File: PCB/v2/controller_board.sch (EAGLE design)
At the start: 30 parts, among them M1 B4B-PH-K-S(LF)(SN), M2 B4B-PH-K-S(LF)(SN), M3 B4B-PH-K-S(LF)(SN), M4 B4B-PH-K-S(LF)(SN)

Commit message: chore(pcb): improve schematics
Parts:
- added R8: 10kR, rcl:R-EU_R0805
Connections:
- net A3 renamed N$24
- removed net N$24 (its old number): D2.A, POWER_CONNECTOR.1
- removed net N$26: D1.A, POWER_CONNECTOR.4
- new net N$22: CONTROLLER.5, R1.2, R8.1, UART_1.2
- net GND: now also D1.A, D2.A, POWER_CONNECTOR.1, POWER_CONNECTOR.4; no longer MC4.!EN
- net UART: now also R8.2; no longer CONTROLLER.5, R1.2, UART_1.2
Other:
- moved on the sheet: 24V_FUSE, 5V_FUSE, CONTROLLER, D1, D2, DEBUG, I2C_1, LED, M1, M2, M3, M4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

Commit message: feat(pcb): add ESD protection
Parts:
- removed DEBUG: B2B-PH-K-S(LF)(SN), B2B-PH-K-S_LF__SN_:B2B-PH-K-S(LF)(SN)
- removed MC1, MC2, MC3, MC4: TMC2209_SILENTSTEPSTICK, TMC2209_SILENTSTEPSTICK:TMC2209_SILENTSTEPSTICK
- added C_M1_A1, C_M1_A2, C_M1_B1, C_M1_B2, C_M2_A1, C_M2_A2, C_M2_A3, C_M2_A4, C_M2_B1, C_M2_B2, C_M2_B3, C_M2_B4, C_M3_A1, C_M3_A2, C_M3_B1, C_M3_B2: 470pF 100V, rcl:C-EUC0402
- added L_M1_A1, L_M1_A2, L_M1_B1, L_M1_B2, L_M2_A1, L_M2_A2, L_M2_A3, L_M2_A4, L_M2_B1, L_M2_B2, L_M2_B3, L_M2_B4, L_M3_A1, L_M3_A2, L_M3_B1, L_M3_B2: 50Ohm@100MHz, ngspice-simulation:L
- added M1_TMC, M2_TMC, M3_TMC, M4_TMC: TMC2209_SILENTSTEPSTICK, TMC2209_SILENTSTEPSTICK:TMC2209_SILENTSTEPSTICK
- added R_M1_A, R_M1_B, R_M2_A, R_M2_A1, R_M2_B, R_M2_B1, R_M3_A, R_M3_B: S1210, varistor:S1210
- CONTROLLER: value TINY2040 -> TINY2040_HEADER; device pimoroni-boards:TINY2040 -> tiny2040_headerd:TINY2040_HEADER
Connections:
- removed net N$18 (its old number): CONTROLLER.SWCLK, DEBUG.2
- new net N$19: L_M1_A2.1, M1_TMC.M2A
- new net N$26: L_M1_A1.1, M1_TMC.M1A
- new net N$27: L_M1_B2.1, M1_TMC.M2B
- new net N$28: L_M2_A1.1, M2_TMC.M1A
- new net N$29: L_M2_A2.1, M2_TMC.M2A
- new net N$30: L_M2_B2.1, M2_TMC.M2B
- new net N$31: L_M2_B1.1, M2_TMC.M1B
- new net N$32: C_M2_A3.2, L_M2_A3.2, M4.1, R_M2_A1.1
- new net N$33: C_M2_A4.2, L_M2_A4.2, M4.2, R_M2_A1.2
- new net N$34: C_M2_B3.2, L_M2_B3.2, M4.3, R_M2_B1.1
- new net N$35: C_M2_B4.2, L_M2_B4.2, M4.4, R_M2_B1.2
- new net N$36: L_M2_A3.1, M4_TMC.M1A
- new net N$37: L_M2_A4.1, M4_TMC.M2A
- new net N$38: L_M2_B4.1, M4_TMC.M2B
- new net N$39: L_M2_B3.1, M4_TMC.M1B
- net 24V: now also M1_TMC.VM, M2_TMC.VM, M3_TMC.VM, M4_TMC.VM; no longer MC1.VM, MC2.VM, MC3.VM, MC4.VM
- net 5V: now also M1_TMC.VIO, M2_TMC.MS1, M2_TMC.VIO, M3_TMC.MS2, M3_TMC.VIO, M4_TMC.MS1, M4_TMC.MS2, M4_TMC.VIO; no longer MC1.VIO, MC2.MS1, MC2.VIO, MC3.MS2, MC3.VIO, MC4.MS1, MC4.MS2, MC4.VIO
- net GND: now also CONTROLLER.GND2, CONTROLLER.GND3, C_M1_A1.1, C_M1_A2.1, C_M1_B1.1, C_M1_B2.1, C_M2_A1.1, C_M2_A2.1, C_M2_A3.1, C_M2_A4.1, C_M2_B1.1, C_M2_B2.1, C_M2_B3.1, C_M2_B4.1, C_M3_A1.1, C_M3_A2.1, C_M3_B1.1, C_M3_B2.1, M1_TMC.!EN, M1_TMC.GND, M1_TMC.MS1, M1_TMC.MS2, M2_TMC.!EN, M2_TMC.GND, M2_TMC.MS2, M3_TMC.!EN, M3_TMC.GND, M3_TMC.MS1, M4_TMC.GND; no longer MC1.!EN, MC1.GND, MC1.MS1, MC1.MS2, MC2.!EN, MC2.GND, MC2.MS2, MC3.!EN, MC3.GND, MC3.MS1, MC4.GND
- net N$1: now also C_M1_A1.2, L_M1_A1.2, R_M1_A.1; no longer MC1.M2A
- net N$10: now also C_M3_A2.2, L_M3_A2.2, M3.2, R_M3_A.2; no longer M3.4, MC3.M1A
- net N$11: now also C_M3_B1.2, L_M3_B1.2, M3.3, R_M3_B.1; no longer M3.2, MC3.M2B
- net N$12: now also C_M3_B2.2, L_M3_B2.2, M3.4, R_M3_B.2; no longer M3.3, MC3.M1B
- net N$13: now also L_M3_A1.1, M3_TMC.M1A; no longer M4.1, MC4.M2A
- net N$14: now also L_M3_A2.1, M3_TMC.M2A; no longer M4.4, MC4.M1A
- net N$15: now also L_M3_B2.1, M3_TMC.M2B; no longer M4.2, MC4.M2B
- net N$16: now also L_M3_B1.1, M3_TMC.M1B; no longer M4.3, MC4.M1B
- net N$2: now also C_M1_A2.2, L_M1_A2.2, R_M1_A.2; no longer MC1.M2B
- net N$21: now also L_M1_B1.1, M1_TMC.M1B; no longer CONTROLLER.SWDIO, DEBUG.1
- net N$3: now also C_M1_B1.2, L_M1_B1.2, R_M1_B.1; no longer MC1.M1B
- net N$4: now also C_M1_B2.2, L_M1_B2.2, R_M1_B.2; no longer MC1.M1A
- net N$5: now also C_M2_A1.2, L_M2_A1.2, R_M2_A.1; no longer MC2.M2A
- net N$6: now also C_M2_A2.2, L_M2_A2.2, M2.2, R_M2_A.2; no longer M2.4, MC2.M1A
- net N$7: now also C_M2_B1.2, L_M2_B1.2, M2.3, R_M2_B.1; no longer M2.2, MC2.M2B
- net N$8: now also C_M2_B2.2, L_M2_B2.2, M2.4, R_M2_B.2; no longer M2.3, MC2.M1B
- net N$9: now also C_M3_A1.2, L_M3_A1.2, R_M3_A.1; no longer MC3.M2A
- net UART: now also M1_TMC.UART, M2_TMC.UART, M3_TMC.UART, M4_TMC.UART; no longer MC1.UART, MC2.UART, MC3.UART, MC4.UART
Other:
- moved on the sheet: 24V_FUSE, 5V_FUSE, CONTROLLER, D1, D2, I2C_1, LED, M1, M2, M3, M4, POWER_CONNECTOR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

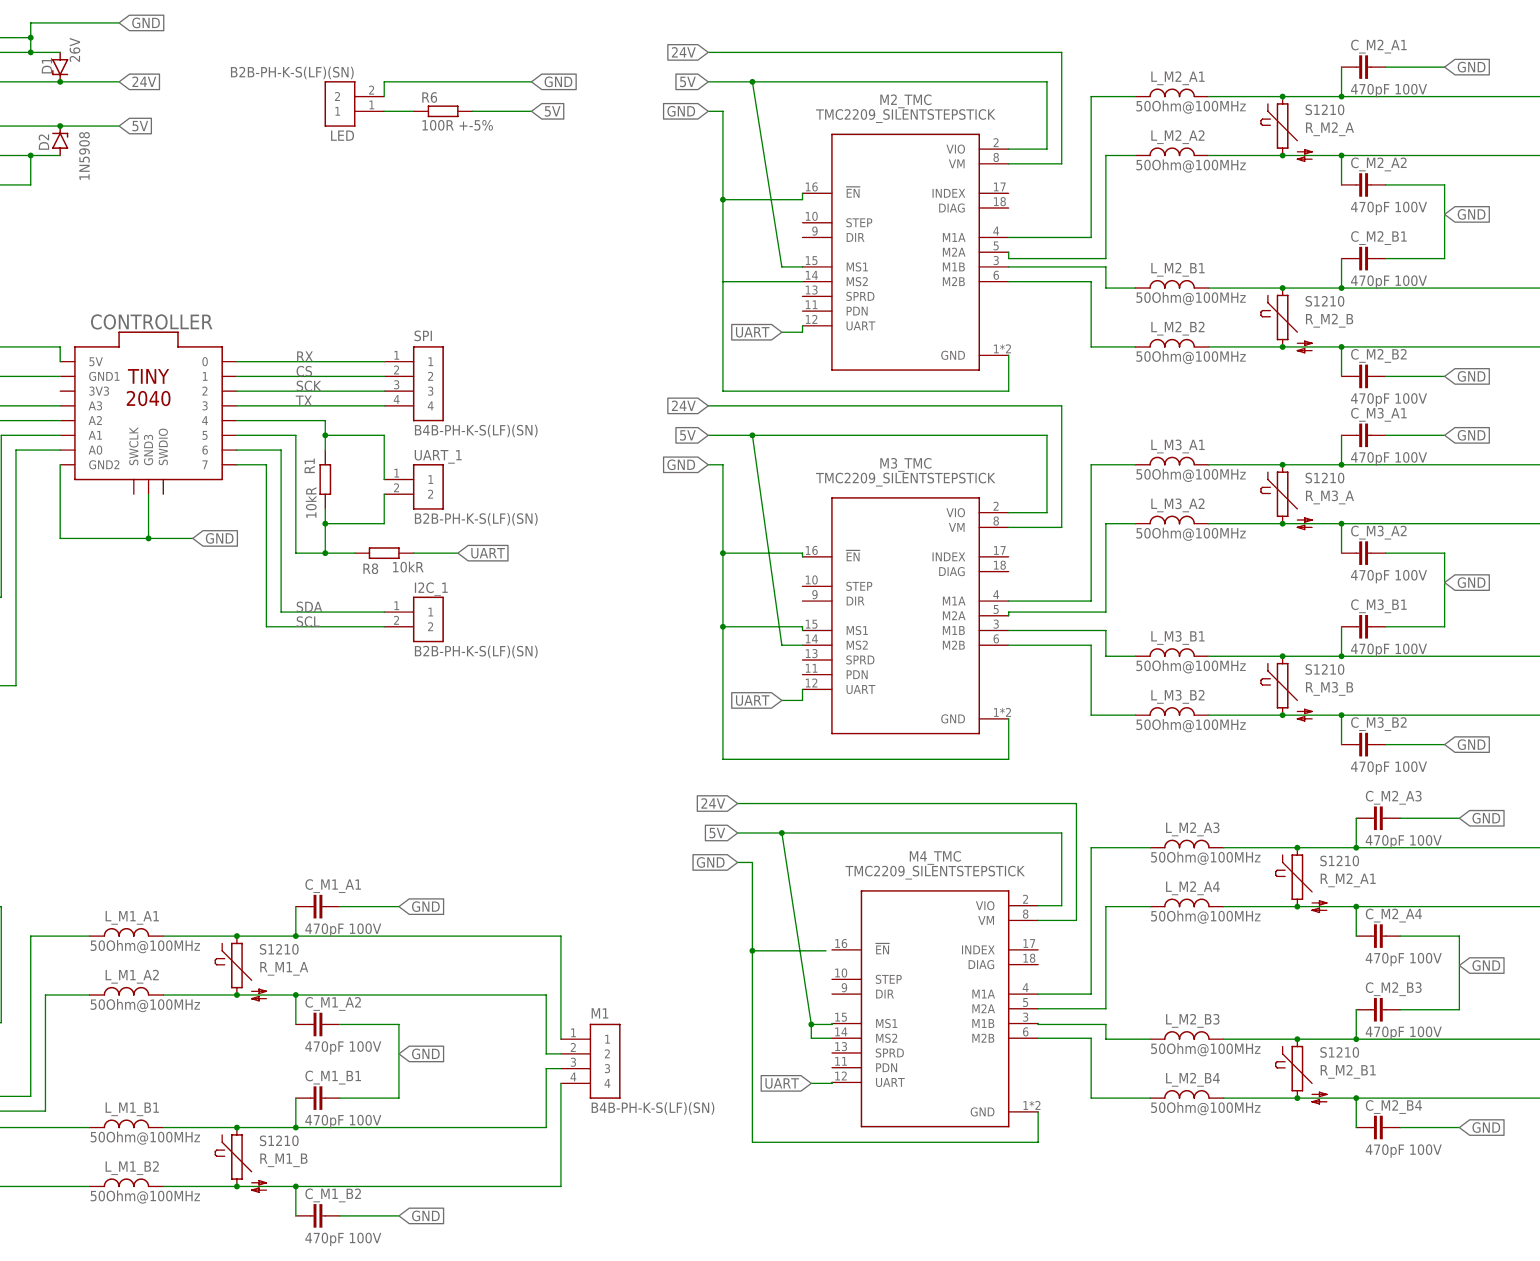
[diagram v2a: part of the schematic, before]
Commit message: feat(pcb): add proper PCB layout
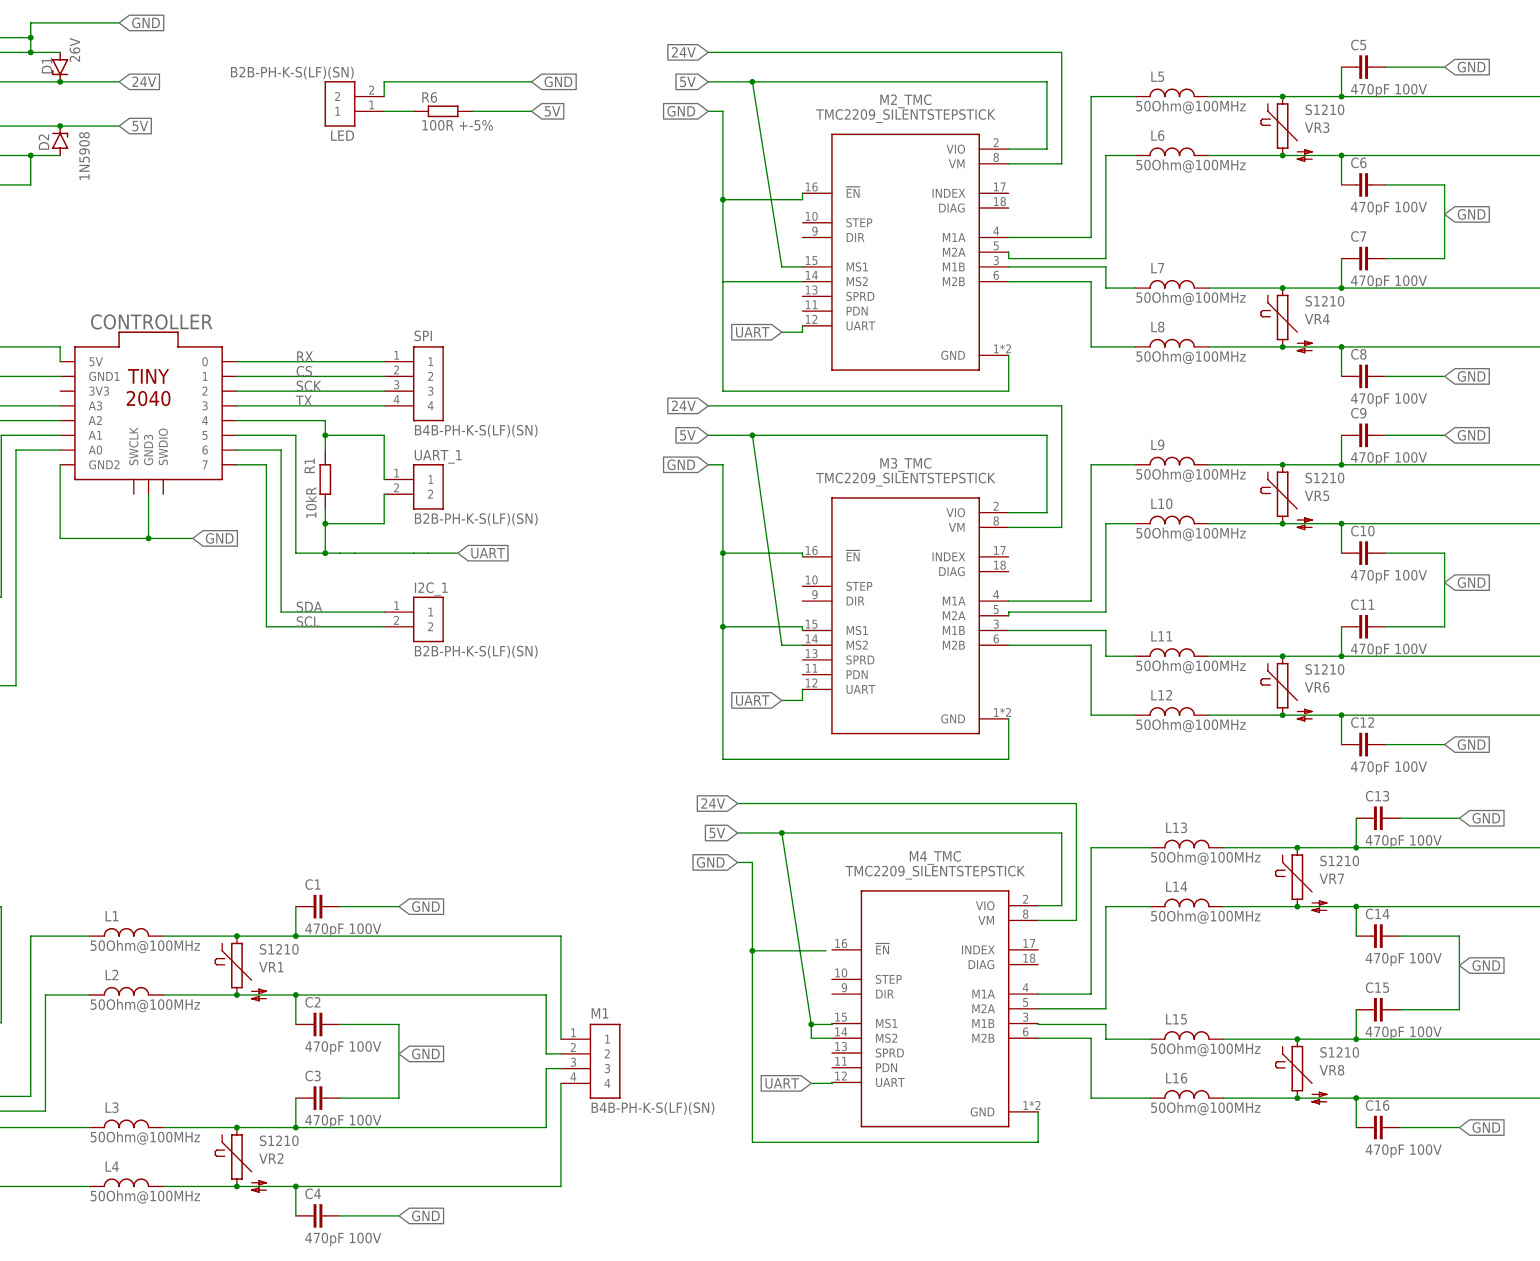
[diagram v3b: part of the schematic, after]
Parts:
- removed R8: 10kR, rcl:R-EU_R0805
- renumbered C_M1_A1 to C1, C_M1_A2 to C2, C_M1_B1 to C3, C_M1_B2 to C4, C_M2_A1 to C5, C_M2_A2 to C6, C_M2_A3 to C13, C_M2_A4 to C14, C_M2_B1 to C7, C_M2_B2 to C8, C_M2_B3 to C15, C_M2_B4 to C16, C_M3_A1 to C9, C_M3_A2 to C10, C_M3_B1 to C11, C_M3_B2 to C12, L_M1_A1 to L1, L_M1_A2 to L2, L_M1_B1 to L3, L_M1_B2 to L4, L_M2_A1 to L5, L_M2_A2 to L6, L_M2_A3 to L13, L_M2_A4 to L14, L_M2_B1 to L7, L_M2_B2 to L8, L_M2_B3 to L15, L_M2_B4 to L16, L_M3_A1 to L9, L_M3_A2 to L10, L_M3_B1 to L11, L_M3_B2 to L12, R_M1_A to VR1, R_M1_B to VR2, R_M2_A to VR3, R_M2_A1 to VR7, R_M2_B to VR4, R_M2_B1 to VR8, R_M3_A to VR5, R_M3_B to VR6
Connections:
- removed net N$22: CONTROLLER.5, R1.2, R8.1, UART_1.2
- net UART: now also CONTROLLER.5, R1.2, UART_1.2; no longer R8.2
